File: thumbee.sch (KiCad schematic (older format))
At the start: 68 parts, among them J1 USB_B, J10 Conn_01x02_Male, J11 Conn_01x02_Male, J12 Conn_02x05_Odd_Even, J2 Conn_01x04_Male, J3 Conn_01x04_Male, J4 Conn_01x02_Male, J5 Conn_01x07_Male, J6 Conn_01x16_Male, J7 Conn_01x04_Male, J8 Conn_01x05_Male, J9 Conn_01x04_Male, U1 msc313e, U2 spinor, U3 ht42b534-1, U4 xc6204xxxxMR, U5 RT8059GJ5, U6 RT8059GJ5, U7 RT8059GJ5, Y1 Crystal

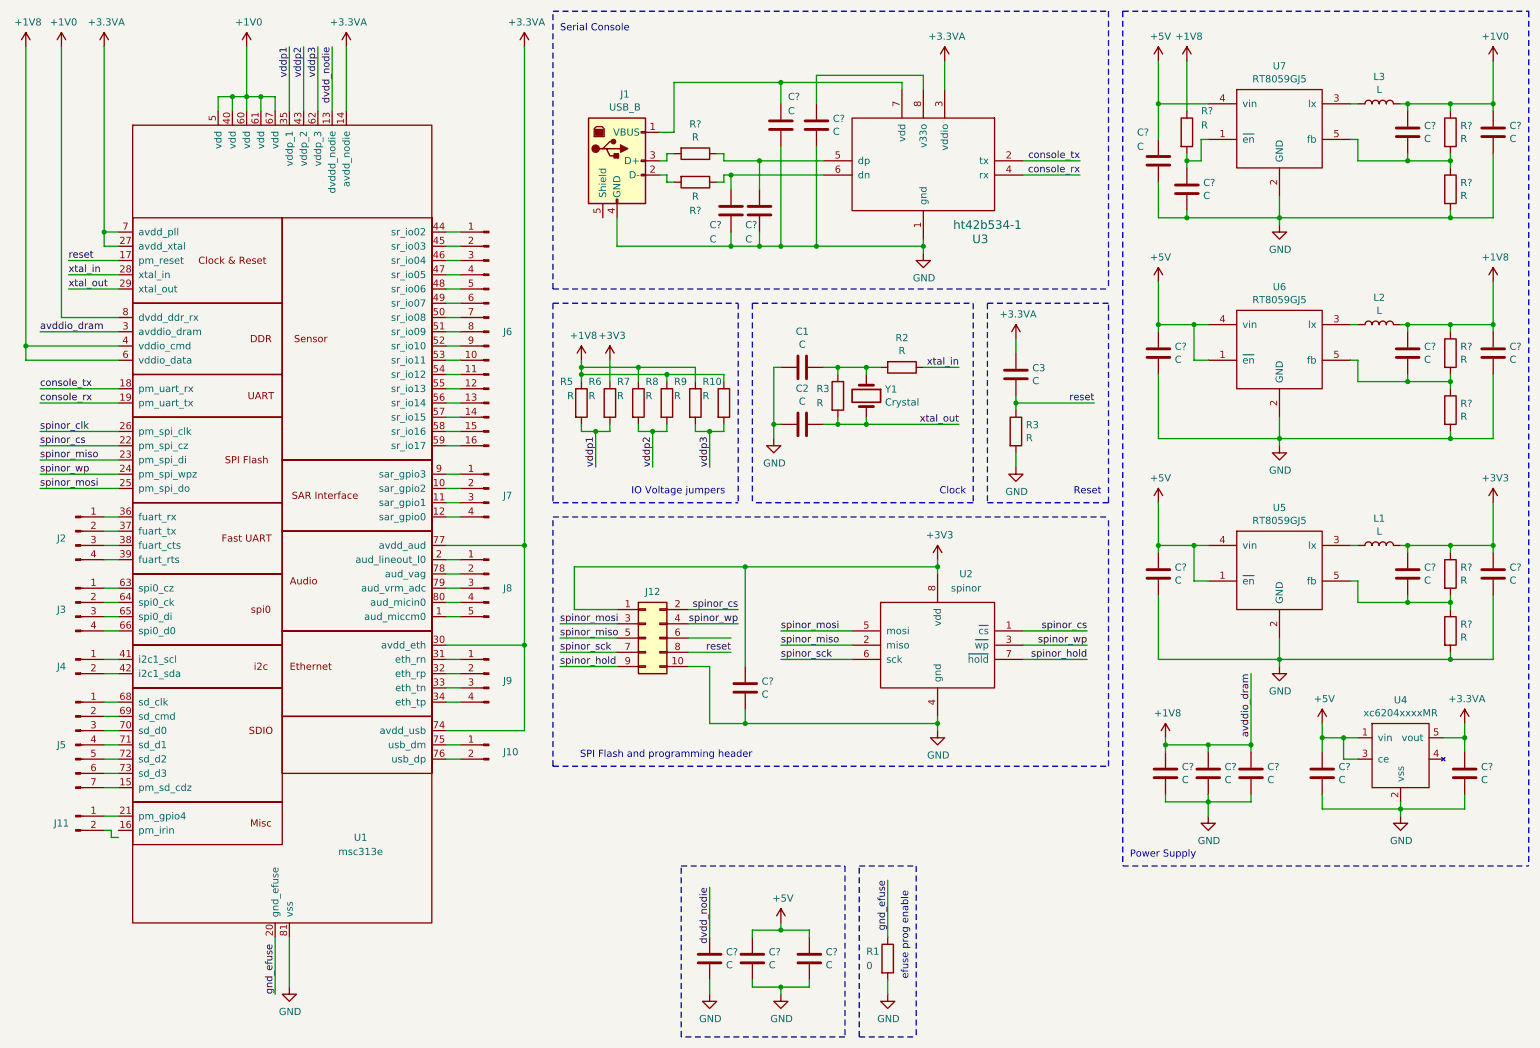
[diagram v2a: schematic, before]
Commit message: Fix schematic bugs. Assign footprints.
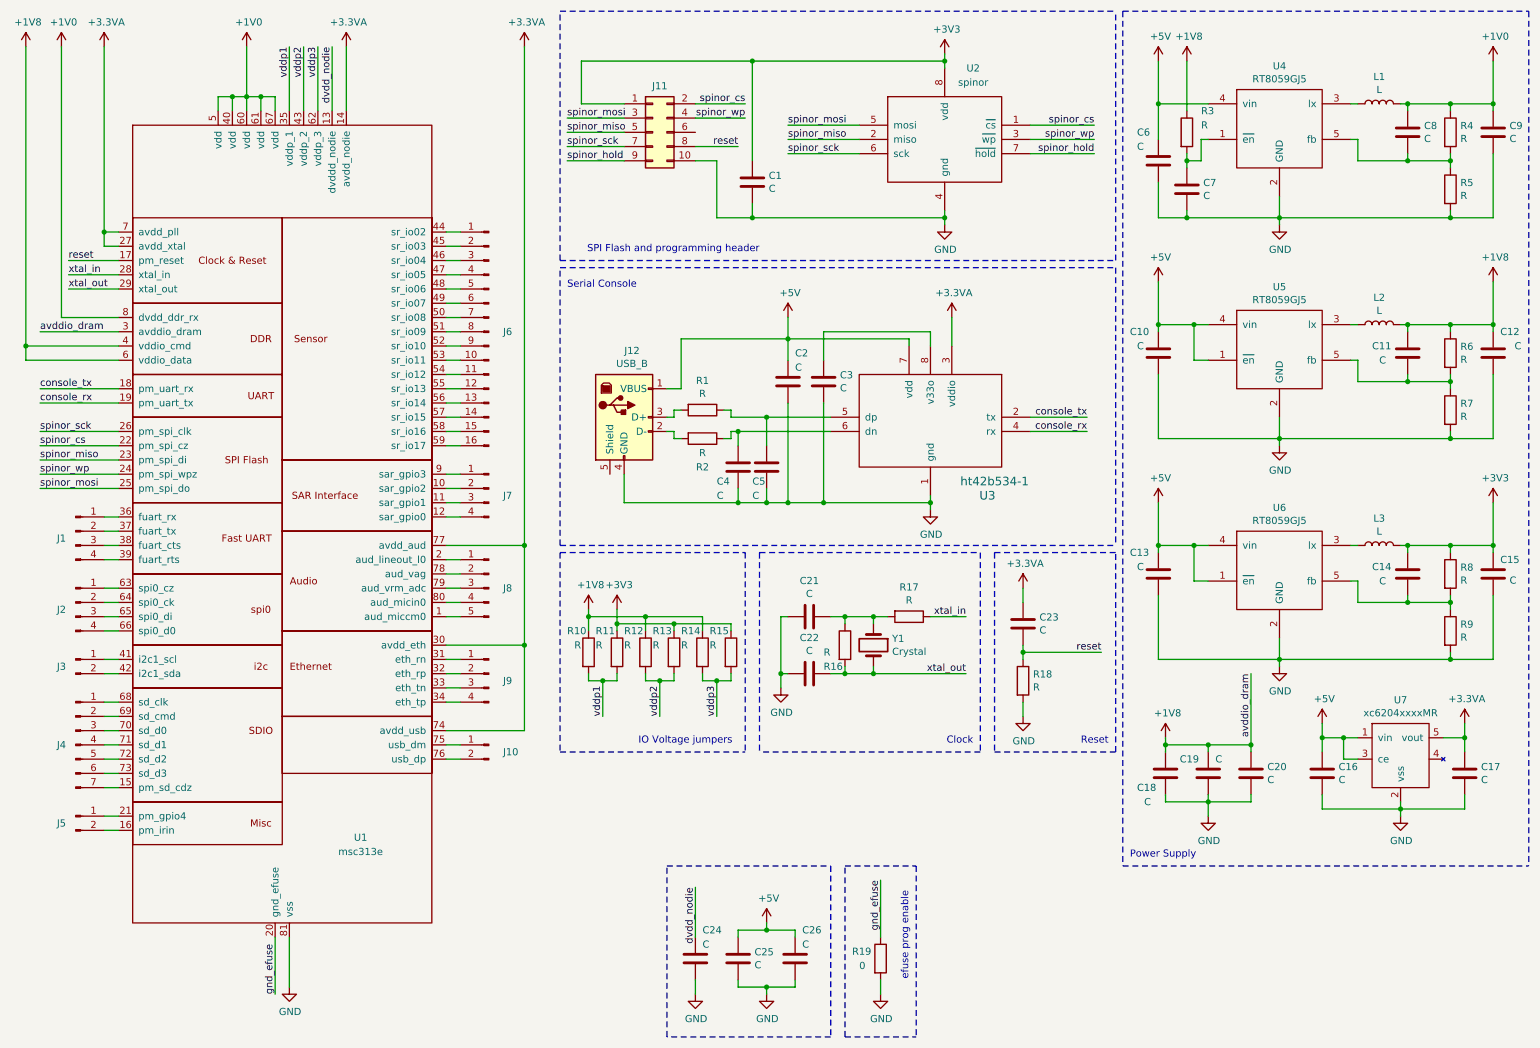
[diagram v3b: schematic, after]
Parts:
- C1, C10, C11, C12, C13, C14, C15, C16, C17, C18, C19, C2, C20, C24, C25, C26, C3, C4, C5, C6, C7, C8, C9: renamed from C?; footprint (none) -> Capacitor_SMD:C_0603_1608Metric
- C21: renamed from C1; footprint (none) -> Capacitor_SMD:C_0603_1608Metric
- C22: renamed from C2; footprint (none) -> Capacitor_SMD:C_0603_1608Metric
- C23: renamed from C3; footprint (none) -> Capacitor_SMD:C_0603_1608Metric
- J1: renamed from J2; footprint (none) -> Connector_PinSocket_2.54mm:PinSocket_1x04_P2.54mm_Vertical
- J10: footprint (none) -> Connector_PinSocket_2.54mm:PinSocket_1x02_P2.54mm_Vertical
- J11: renamed from J12; footprint (none) -> Connector_PinSocket_2.54mm:PinSocket_2x05_P2.54mm_Vertical
- J12: renamed from J1; footprint (none) -> USB-MICRO-MK5P-2:USB-MICRO-B
- J2: renamed from J3; footprint (none) -> Connector_PinSocket_2.54mm:PinSocket_1x04_P2.54mm_Vertical
- J3: renamed from J4; footprint (none) -> Connector_PinSocket_2.54mm:PinSocket_1x02_P2.54mm_Vertical
- J4: renamed from J5; footprint (none) -> Connector_PinSocket_2.54mm:PinSocket_1x07_P2.54mm_Vertical
- J5: renamed from J11; footprint (none) -> Connector_PinSocket_2.54mm:PinSocket_1x02_P2.54mm_Vertical
- J6: footprint (none) -> Connector_PinSocket_2.54mm:PinSocket_1x16_P2.54mm_Vertical
- J7, J9: footprint (none) -> Connector_PinSocket_2.54mm:PinSocket_1x04_P2.54mm_Vertical
- J8: footprint (none) -> Connector_PinSocket_2.54mm:PinSocket_1x05_P2.54mm_Vertical
- L1: renamed from L3; footprint (none) -> cd32:CD32
- L2: footprint (none) -> cd32:CD32
- L3: renamed from L1; footprint (none) -> cd32:CD32
- R1, R2, R3, R4, R5, R6, R7, R8, R9: renamed from R?; footprint (none) -> Resistor_SMD:R_0603_1608Metric
- R10: renamed from R5; footprint (none) -> Resistor_SMD:R_0603_1608Metric
- R11: renamed from R6; footprint (none) -> Resistor_SMD:R_0603_1608Metric
- R12: renamed from R7; footprint (none) -> Resistor_SMD:R_0603_1608Metric
- R13: renamed from R8; footprint (none) -> Resistor_SMD:R_0603_1608Metric
- R14: renamed from R9; footprint (none) -> Resistor_SMD:R_0603_1608Metric
- R15: renamed from R10; footprint (none) -> Resistor_SMD:R_0603_1608Metric
- R16, R18: renamed from R3; footprint (none) -> Resistor_SMD:R_0603_1608Metric
- R17: renamed from R2; footprint (none) -> Resistor_SMD:R_0603_1608Metric
- R19: renamed from R1; footprint (none) -> Resistor_SMD:R_0603_1608Metric
- U2: footprint (none) -> wson8-8x6mm:wson8-8x6mm
- U3: footprint (none) -> Package_SO:SOIC-8_3.9x4.9mm_P1.27mm
- U4: renamed from U7; footprint (none) -> Package_TO_SOT_SMD:TSOT-23-5
- U5: renamed from U6; footprint (none) -> Package_TO_SOT_SMD:TSOT-23-5
- U6: renamed from U5; footprint (none) -> Package_TO_SOT_SMD:TSOT-23-5
- U7: renamed from U4; footprint (none) -> Package_TO_SOT_SMD:TSOT-23-5
- Y1: footprint (none) -> Crystal:Crystal_SMD_5032-2Pin_5.0x3.2mm
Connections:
- net spinor_clk is gone; now on net spinor_sck: U1.26 (pm_spi_clk)
- net +1V8: no longer R13.1, R15.1
- net +3V3: now also R13.1, R15.1
- net +5V: now also C2.1, J12.1 (VBUS), U3.7 (vdd)
- net at U1.16 (pm_irin): now also J5.2 (Pin_2)
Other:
- moved on the sheet: C1, C2, C21, C22, C23, C24, C25, C26, C3, C4, C5, J11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

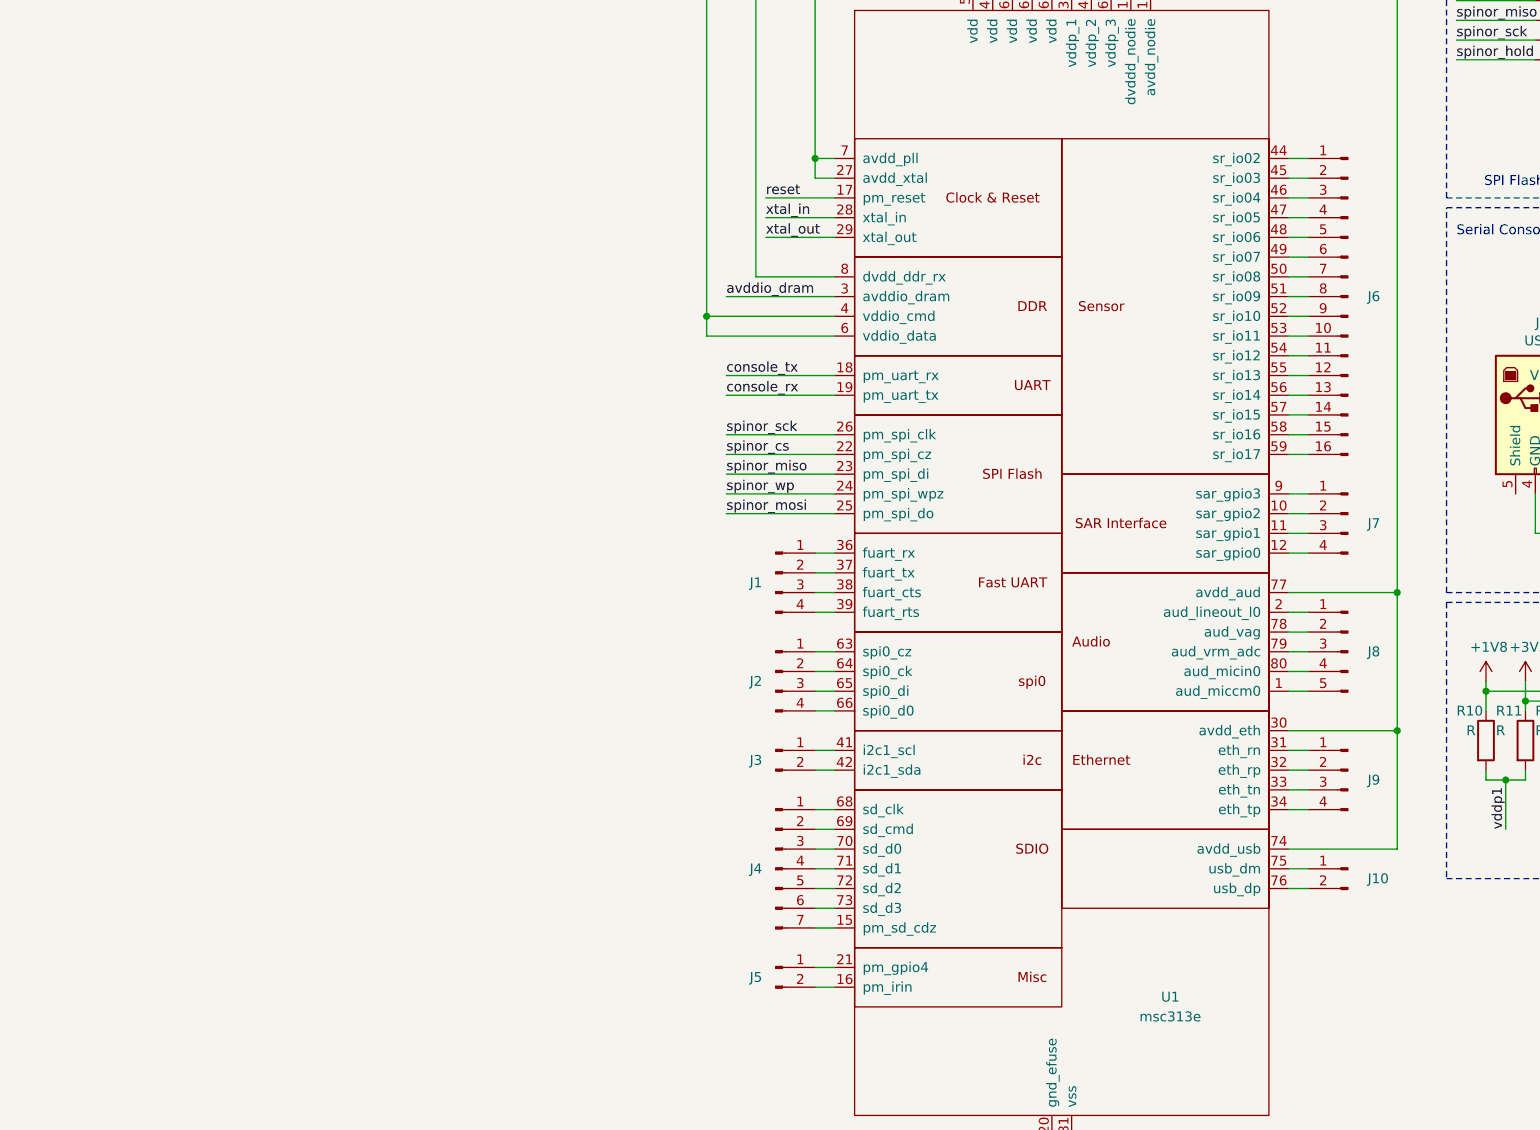
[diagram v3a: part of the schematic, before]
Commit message: QFN footprint fix up. Replace headers with a module footprint. Very rought parts layout and some routing.
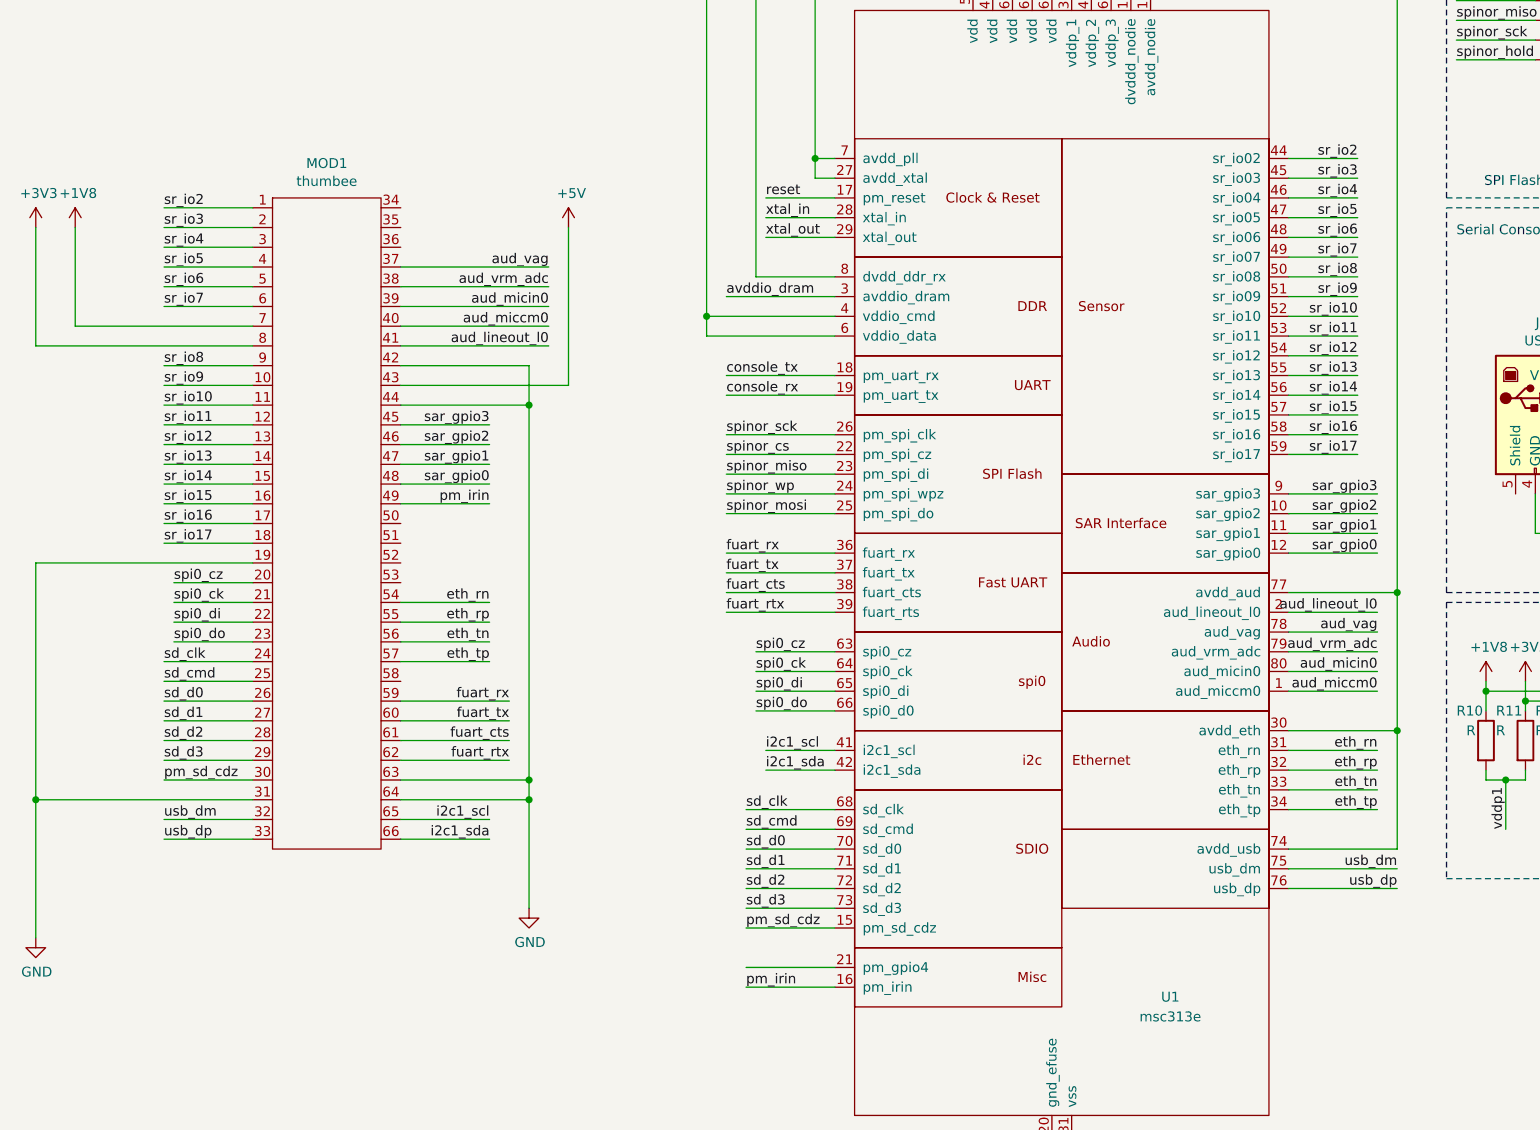
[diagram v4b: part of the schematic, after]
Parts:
- removed J1, J2, J7, J9: Conn_01x04_Male, Connector_PinSocket_2.54mm:PinSocket_1x04_P2.54mm_Vertical, symbol Connector:Conn_01x04_Male
- removed J10, J3, J5: Conn_01x02_Male, Connector_PinSocket_2.54mm:PinSocket_1x02_P2.54mm_Vertical, symbol Connector:Conn_01x02_Male
- removed J4: Conn_01x07_Male, Connector_PinSocket_2.54mm:PinSocket_1x07_P2.54mm_Vertical, symbol Connector:Conn_01x07_Male
- removed J6: Conn_01x16_Male, Connector_PinSocket_2.54mm:PinSocket_1x16_P2.54mm_Vertical, symbol Connector:Conn_01x16_Male
- removed J8: Conn_01x05_Male, Connector_PinSocket_2.54mm:PinSocket_1x05_P2.54mm_Vertical, symbol Connector:Conn_01x05_Male
- added MOD1: thumbee, thumbee:thumbee, symbol thumbee:thumbee
- J11: footprint Connector_PinSocket_2.54mm:PinSocket_2x05_P2.54mm_Vertical -> Connector_PinHeader_1.00mm:PinHeader_2x05_P1.00mm_Vertical_SMD
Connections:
- net +1V8: now also MOD1.7
- net +3V3: now also MOD1.8
- net +5V: now also MOD1.43
- net GND: now also MOD1.19, MOD1.31, MOD1.42, MOD1.44, MOD1.63, MOD1.64
- net aud_miccm0: now reaches U1.1 (aud_miccm0)
- net aud_miccm0: now also MOD1.40
- net sar_gpio2: now reaches U1.10 (sar_gpio2)
- net sar_gpio2: now also MOD1.46
- net sar_gpio1: now reaches U1.11 (sar_gpio1)
- net sar_gpio1: now also MOD1.47
- net sar_gpio0: now reaches U1.12 (sar_gpio0)
- net sar_gpio0: now also MOD1.48
- net pm_sd_cdz: now reaches U1.15 (pm_sd_cdz)
- net pm_sd_cdz: now also MOD1.30
- net pm_irin: now reaches U1.16 (pm_irin)
- net pm_irin: now also MOD1.49
- net aud_lineout_l0: now reaches U1.2 (aud_lineout_l0)
- net aud_lineout_l0: now also MOD1.41
- net eth_rn: now reaches U1.31 (eth_rn)
- net eth_rn: now also MOD1.54
- net eth_rp: now reaches U1.32 (eth_rp)
- net eth_rp: now also MOD1.55
- net eth_tn: now reaches U1.33 (eth_tn)
- net eth_tn: now also MOD1.56
- net eth_tp: now reaches U1.34 (eth_tp)
- net eth_tp: now also MOD1.57
- net fuart_rx: now reaches U1.36 (fuart_rx)
- net fuart_rx: now also MOD1.59
- net fuart_tx: now reaches U1.37 (fuart_tx)
- net fuart_tx: now also MOD1.60
- net fuart_cts: now reaches U1.38 (fuart_cts)
- net fuart_cts: now also MOD1.61
- net fuart_rtx: now reaches U1.39 (fuart_rts)
- net fuart_rtx: now also MOD1.62
- net i2c1_scl: now reaches U1.41 (i2c1_scl)
- net i2c1_scl: now also MOD1.65
- net i2c1_sda: now reaches U1.42 (i2c1_sda)
- net i2c1_sda: now also MOD1.66
- net sr_io2: now reaches U1.44 (sr_io02)
- net sr_io2: now also MOD1.1
- net sr_io3: now reaches U1.45 (sr_io03)
- net sr_io3: now also MOD1.2
- net sr_io4: now reaches U1.46 (sr_io04)
- net sr_io4: now also MOD1.3
- net sr_io5: now reaches U1.47 (sr_io05)
- net sr_io5: now also MOD1.4
- net sr_io6: now reaches U1.48 (sr_io06)
- net sr_io6: now also MOD1.5
- net sr_io7: now reaches U1.49 (sr_io07)
- net sr_io7: now also MOD1.6
- net sr_io8: now reaches U1.50 (sr_io08)
- net sr_io8: now also MOD1.9
- net sr_io9: now reaches U1.51 (sr_io09)
- net sr_io9: now also MOD1.10
- net sr_io10: now reaches U1.52 (sr_io10)
- net sr_io10: now also MOD1.11
- net sr_io11: now reaches U1.53 (sr_io11)
- net sr_io11: now also MOD1.12
- net sr_io12: now reaches U1.54 (sr_io12)
- net sr_io12: now also MOD1.13
- net sr_io13: now reaches U1.55 (sr_io13)
- net sr_io13: now also MOD1.14
- net sr_io14: now reaches U1.56 (sr_io14)
- net sr_io14: now also MOD1.15
- net sr_io15: now reaches U1.57 (sr_io15)
- net sr_io15: now also MOD1.16
- net sr_io16: now reaches U1.58 (sr_io16)
- net sr_io16: now also MOD1.17
- net sr_io17: now reaches U1.59 (sr_io17)
- net sr_io17: now also MOD1.18
- net spi0_cz: now reaches U1.63 (spi0_cz)
- net spi0_cz: now also MOD1.20
- net spi0_ck: now reaches U1.64 (spi0_ck)
- net spi0_ck: now also MOD1.21
- net spi0_di: now reaches U1.65 (spi0_di)
- net spi0_di: now also MOD1.22
- net spi0_do: now reaches U1.66 (spi0_d0)
- net spi0_do: now also MOD1.23
- net sd_clk: now reaches U1.68 (sd_clk)
- net sd_clk: now also MOD1.24
- net sd_cmd: now reaches U1.69 (sd_cmd)
- net sd_cmd: now also MOD1.25
- net sd_d0: now reaches U1.70 (sd_d0)
- net sd_d0: now also MOD1.26
- net sd_d1: now reaches U1.71 (sd_d1)
- net sd_d1: now also MOD1.27
- net sd_d2: now reaches U1.72 (sd_d2)
- net sd_d2: now also MOD1.28
- net sd_d3: now reaches U1.73 (sd_d3)
- net sd_d3: now also MOD1.29
- net usb_dm: now reaches U1.75 (usb_dm)
- net usb_dm: now also MOD1.32
- net usb_dp: now reaches U1.76 (usb_dp)
- net usb_dp: now also MOD1.33
- net aud_vag: now reaches U1.78 (aud_vag)
- net aud_vag: now also MOD1.37
- net aud_vrm_adc: now reaches U1.79 (aud_vrm_adc)
- net aud_vrm_adc: now also MOD1.38
- net aud_micin0: now reaches U1.80 (aud_micin0)
- net aud_micin0: now also MOD1.39
- net sar_gpio3: now reaches U1.9 (sar_gpio3)
- net sar_gpio3: now also MOD1.45

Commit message: Rough all routed.
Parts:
- added C27: C, Capacitor_SMD:C_0603_1608Metric, symbol Device:C
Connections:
- net +1V0: now also C27.1
- net GND: now also MOD1.34, MOD1.35, MOD1.36, MOD1.51, MOD1.52, MOD1.53, MOD1.58, C27.2
- net spinor_hold: now also J11.3 (Pin_3); no longer J11.9 (Pin_9)
- net spinor_miso: now also J11.4 (Pin_4); no longer J11.5 (Pin_5)
- net spinor_mosi: now also J11.7 (Pin_7); no longer J11.3 (Pin_3)
- net spinor_sck: now also J11.5 (Pin_5); no longer J11.7 (Pin_7)
- net spinor_wp: now also J11.6 (Pin_6); no longer J11.4 (Pin_4)
- net pm_gpio4: now reaches U1.21 (pm_gpio4)
- net pm_gpio4: now also MOD1.50
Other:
- moved on the sheet: MOD1
